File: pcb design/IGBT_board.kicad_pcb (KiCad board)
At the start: 4 copper layers, 150 x 100 mm, 238 parts, among them J1 4-794627-0, J2 DESAT, J3 DESAT, Q1 IGBT, Q10 IGBT, Q11 IGBT, Q12 IGBT, Q13 NPN, Q14 PNP, Q15 CSD19533Q5A, Q16 CSD19533Q5A, Q17 NPN, Q18 PNP, Q19 PNP, Q2 IGBT, Q20 PNP, Q3 IGBT, Q4 IGBT, Q5 IGBT, Q6 IGBT, Q7 IGBT, Q8 IGBT, Q9 IGBT, T1 TRANS-3-1CT, U1 ISO5852S, U11 TLP2745, U12 OPA2172, U2 LM5030, U3 ISO5852S, U4 NAND, U5 APE8865U5-33-HF-3, U6 NAND, U7 NAND, U8 TLP2745, U9 OPA2172

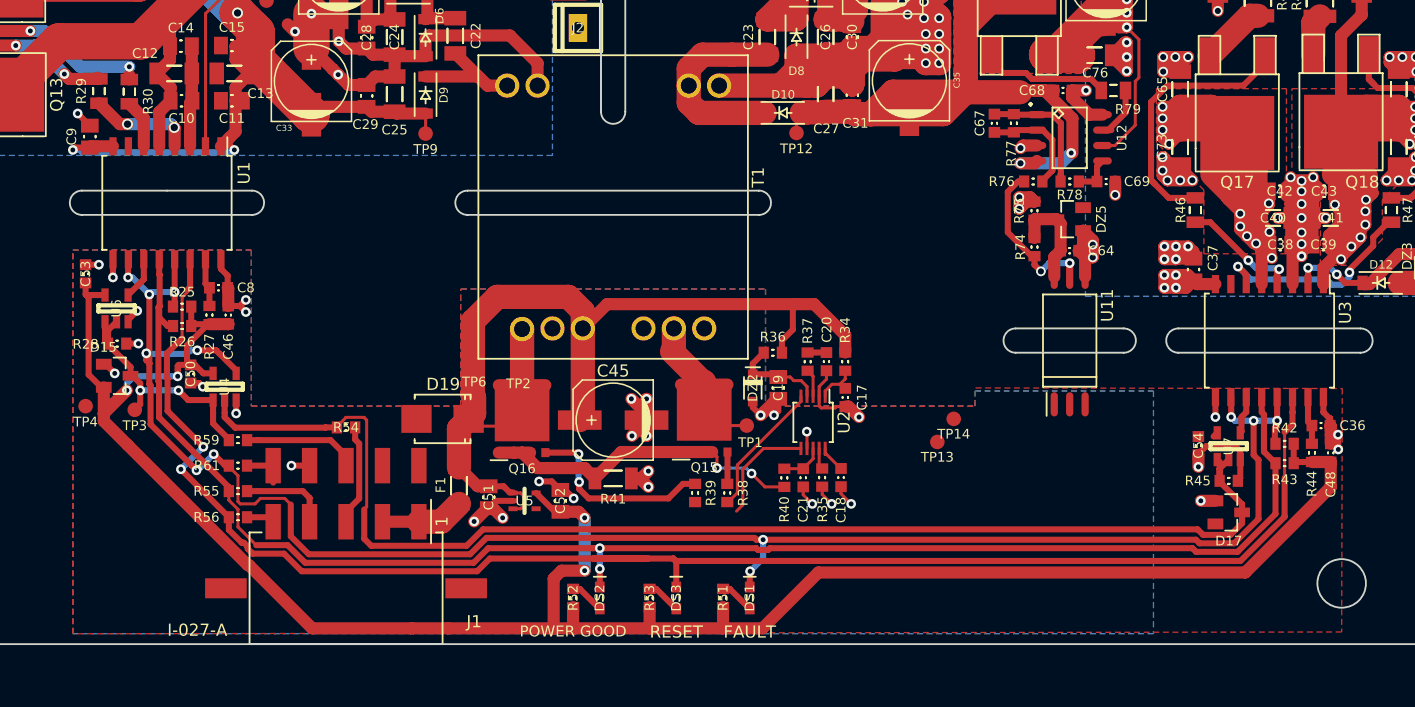
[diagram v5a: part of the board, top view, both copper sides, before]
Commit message: Phase voltage sensing laid out
Signed-off-by: Marcos Chaparro <mchaparro@paltatech.com>
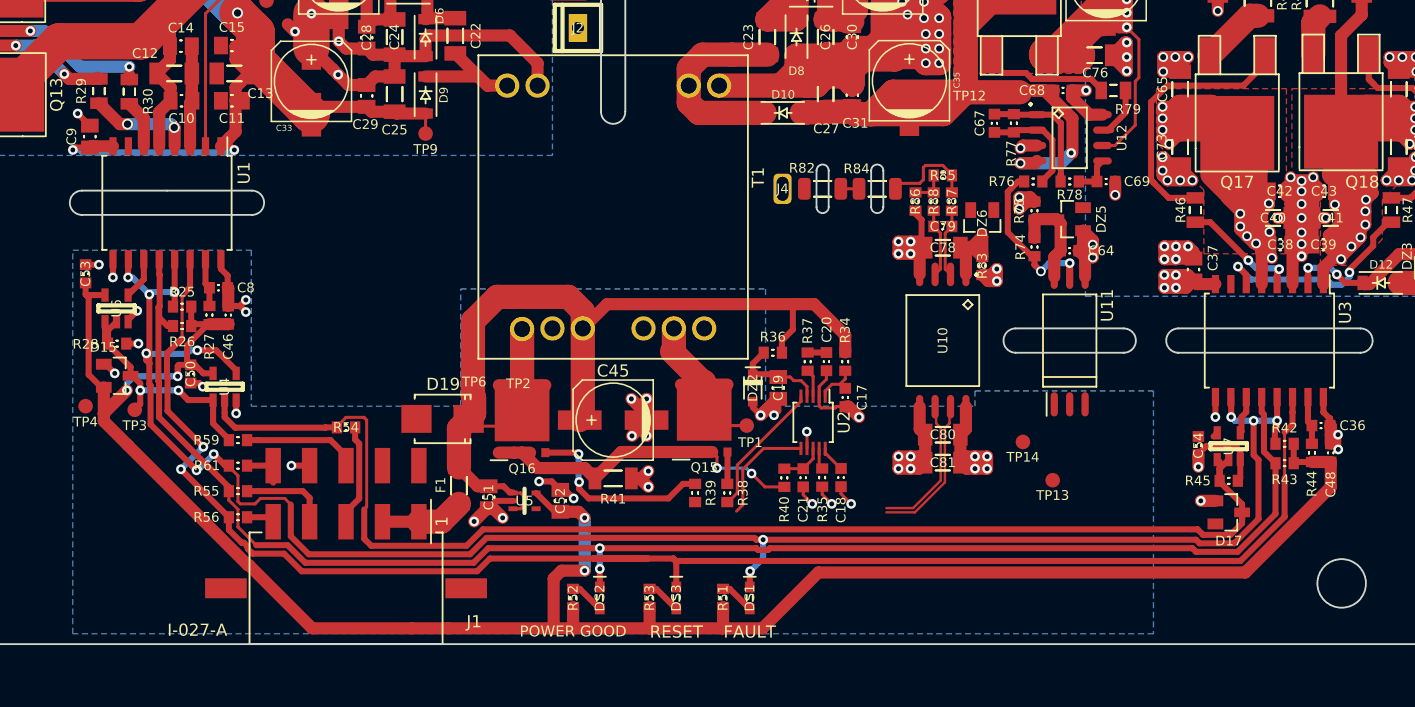
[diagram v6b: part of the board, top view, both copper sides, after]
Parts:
- added C78: 100nF, IPC7351-Nominal:CAPC3216X70, F.Cu at (27.1, 17.4)
- added C79: 330pF, IPC7351-Nominal:CAPC1608X55, F.Cu at (27.1, 15.6)
- added C80: 100nF, IPC7351-Nominal:CAPC3216X70, F.Cu at (27.1, 32.8)
- added C81: 1uF, IPC7351-Nominal:CAPC3216X70, F.Cu at (27.1, 35.0)
- added DZ6: 5v, smd-semi:SOT-23, F.Cu at (30.4, 15.3)
- added J4: PHASE, conn-100mil:CONN-100MIL-F-1x1, F.Cu at (13.9, 12.5)
- added R82: 1M, IPC7351-Nominal:RESC3216X60, F.Cu at (17.2, 12.5)
- added R83: 12R, IPC7351-Nominal:RESC1608X50, F.Cu at (30.4, 18.9)
- added R84: 1M, IPC7351-Nominal:RESC3216X60, F.Cu at (21.8, 12.5)
- added R85: 1k, IPC7351-Nominal:RESC1608X50, F.Cu at (27.1, 11.4)
- added R86: 10k, IPC7351-Nominal:RESC1608X50, F.Cu at (24.9, 13.6)
- added R87: 12R, IPC7351-Nominal:RESC1608X50, F.Cu at (27.9, 13.6)
- added R88: 12R, IPC7351-Nominal:RESC1608X50, F.Cu at (26.4, 13.6)
- added U10: AMC1200, IPC7351-Nominal:SOIC127P1032X265-8, F.Cu at (27.1, 25.0)
- moved TP12 14.9 mm to (29.4, 3.55)
- moved TP13 10.0 mm to (36.2, 36.5)
- moved TP14 6.01 mm to (33.8, 33.4)
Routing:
- net /phase voltage/Vout+: track 0.00 -> 12.3 mm
- net /phase voltage/Vout-: track 0.00 -> 11.7 mm
- net VBUS-: track 667.0 -> 678.6 mm, vias 71 -> 75
- net 3.3v: track 177.9 -> 188.5 mm, vias 4 -> 8
- net GND: track 72.1 -> 82.7 mm, vias 32 -> 36
- net Net-(C78-Pad2): track 0.00 -> 8.32 mm
- net Net-(R84-Pad1): track 0.00 -> 7.82 mm
- net /phase voltage/VIN-: track 0.00 -> 5.81 mm
- net /phase voltage/VIN+: track 0.00 -> 5.66 mm
- net /IGBT_driver_BOT/+15V: track 107.8 -> 111.7 mm, vias 22 -> 24
- net Net-(R85-Pad2): track 0.00 -> 2.90 mm
- net /IGBT_driver_BOT/-8V: track 68.0 -> 66.4 mm
- net Net-(R82-Pad1): track 0.00 -> 1.50 mm
- removed copper zone on F.Cu, net GND
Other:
- outline, holes or cut-outs redrawn

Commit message: Added mounting points, trying 12 pos connector. Added 3d models
Signed-off-by: Marcos Chaparro <mchaparro@paltatech.com>
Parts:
- removed C55, C63: 1nF, IPC7351-Nominal:CAPC1608X55
- removed C56: 1uF, IPC7351-Nominal:CAPC1608X55
- removed C57, C58, C71, C72, C75: 10uF 50v, IPC7351-Nominal:CAPC3216X70
- removed C59, C61: 10nF, IPC7351-Nominal:CAPC1608X55
- removed C60: 100nF, IPC7351-Nominal:CAPC1608X55
- removed C62: 47uF 50v, w_smd_cap:c_elec_6.3x7.7
- removed DS4: CAPS_CHARGED, smd-semi:LED-0603
- removed DZ4: 10v, smd-semi:SOT-23
- removed the G*** at (136.8, -17.4)
- removed J1: 4-794627-0, paltatech:TE-4-794627-0
- removed Q19: PNP, SMD_Packages:DPAK-2
- removed R62, R63, R66: 50k 1W, IPC7351-Nominal:RESC6432X70
- removed R68: 380R, IPC7351-Nominal:RESC1608X50
- removed R69: 470R, IPC7351-Nominal:RESC1608X50
- removed R70, R71, R72: 10k, IPC7351-Nominal:RESC1608X50
- removed R73: 100R, IPC7351-Nominal:RESC2012X50
- removed U8: TLP2745, paltatech:SDIP6
- removed U9: OPA2172, IPC7351-Nominal:SOIC127P600X175-8
- added HOLE102: MOUNTING_HOLE, paltatech:SMD_STANDOFF_M3, F.Cu at (-33.0, 45.0)
- added HOLE102: MOUNTING_HOLE, paltatech:SMD_STANDOFF_M3, F.Cu at (-58.0, 45.0)
- added REF**: inverter_support2, inverter_support2, F.Cu at (0.00, 50.0)
- added REF**: MountingHole_6mm, Mounting_Holes:MountingHole_4mm, F.Cu at (76.5, -32.0)
- added REF**: MountingHole_6mm, Mounting_Holes:MountingHole_4mm, F.Cu at (-76.5, -32.0)
- added REF**: Pin_Header_Straight_2x06, Pin_Headers:Pin_Header_Straight_2x06, F.Cu at (-51.9, 46.1)
- MP1: footprint paltatech:heatsink-watercooled-20x210mm -> heatsink-watercooled-20x210mm
- moved R60 20.1 mm to (-72.0, -17.9), turned to 0 degrees
- moved C47 15.5 mm to (-72.0, -20.4), turned to 180 degrees
- moved DZ2 7.73 mm to (13.6, 36.4)
- moved C21 3.90 mm to (15.6, 40.2)
- moved R40 3.90 mm to (14.1, 40.2)
- moved C20 3.90 mm to (17.5, 30.6)
- moved R34 3.90 mm to (19.1, 30.6)
- moved R37 3.90 mm to (16.0, 30.6)
- moved U2 3.90 mm to (16.4, 35.6)
- moved C17 3.90 mm to (19.1, 33.6)
- moved C18 3.90 mm to (18.7, 40.2)
- moved C19 3.90 mm to (13.6, 32.8)
- moved R35 3.90 mm to (17.2, 40.2)
- moved R36 3.90 mm to (13.1, 29.9)
- moved TP1 3.90 mm to (10.9, 35.9)
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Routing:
- net 24v: track 72.2 -> 42.8 mm
- net Net-(R48-Pad1): track 1.70 -> 13.9 mm
- net PHASE: track 300.0 -> 288.6 mm, vias 9 -> 7
- net Net-(R49-Pad1): track 1.70 -> 11.0 mm
- net VBUS-: track 678.6 -> 687.3 mm, vias 75 -> 76
- net Net-(R38-Pad2): track 11.3 -> 3.86 mm
- net /IGBT_driver_BOT/-VEE: track 110.9 -> 116.3 mm
- net (no net): track 0.00 -> 4.28 mm, vias 0 -> 4
- net GND: track 82.7 -> 78.6 mm, vias 36 -> 32
- net Net-(R39-Pad1): track 9.16 -> 8.44 mm
- net Net-(C19-Pad1): track 7.83 -> 8.33 mm, vias 0 -> 1
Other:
- board size 150 x 100 mm -> 162 x 100 mm

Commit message: Added comments before I forget things, changed X5R to X7R. Updated PCB
Signed-off-by: Marcos Chaparro <mchaparro@paltatech.com>
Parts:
- added C55: 1nF, IPC7351-Nominal:CAPC1608X55, F.Cu at (181.2, 24.1)
- added C56: 1uF, IPC7351-Nominal:CAPC1608X55, F.Cu at (165.7, 41.0)
- added C57: 10uF 50v, IPC7351-Nominal:CAPC3216X70, F.Cu at (151.2, 40.3)
- added C58: 10uF 50v, IPC7351-Nominal:CAPC3216X70, F.Cu at (158.9, 33.7)
- added C59: 10nF, IPC7351-Nominal:CAPC1608X55, F.Cu at (172.4, 3.87)
- added C60: 100nF, IPC7351-Nominal:CAPC1608X55, F.Cu at (178.9, -1.13)
- added C61: 10nF, IPC7351-Nominal:CAPC1608X55, F.Cu at (170.8, 10.5)
- added C62: 47uF 50v, w_smd_cap:c_elec_6.3x7.7, F.Cu at (163.4, 2.45)
- added C63: 1nF, IPC7351-Nominal:CAPC1608X55, F.Cu at (134.1, 38.9)
- added C71: 10uF 50v, IPC7351-Nominal:CAPC3216X70, F.Cu at (166.7, 24.5)
- added C72: 10uF 50v, IPC7351-Nominal:CAPC3216X70, F.Cu at (166.7, 29.8)
- added C75: 10uF 50v, IPC7351-Nominal:CAPC3216X70, F.Cu at (151.2, 15.2)
- added C77: 100pF, IPC7351-Nominal:CAPC1608X55, F.Cu at (131.1, 30.9)
- added C82: 100pF, IPC7351-Nominal:CAPC1608X55, F.Cu at (137.0, 30.9)
- added C83: 100nF, IPC7351-Nominal:CAPC1608X55, F.Cu at (173.5, 30.3)
- added C84: 100nF, IPC7351-Nominal:CAPC1608X55, F.Cu at (134.1, 43.4)
- added DS4: CAPS_CHARGED, smd-semi:LED-0603, F.Cu at (122.0, 31.0)
- added Q19: PNP, SMD_Packages:DPAK-2, F.Cu at (152.4, 9.29)
- added R62: 50k 1W, IPC7351-Nominal:RESC6432X70, F.Cu at (133.0, 7.05)
- added R63: 50k 1W, IPC7351-Nominal:RESC6432X70, F.Cu at (133.0, 14.0)
- added R66: 50k 1W, IPC7351-Nominal:RESC6432X70, F.Cu at (133.0, 0.10)
- added R68: 380R, IPC7351-Nominal:RESC1608X50, F.Cu at (173.4, 34.8)
- added R69: NI, IPC7351-Nominal:RESC3216X60, F.Cu at (166.6, 35.6)
- added R70: 10k, IPC7351-Nominal:RESC1608X50, F.Cu at (176.8, 8.40)
- added R71: 10k, IPC7351-Nominal:RESC1608X50, F.Cu at (178.9, 3.40)
- added R72: 10k, IPC7351-Nominal:RESC1608X50, F.Cu at (170.8, 15.0)
- added R73: 100R, IPC7351-Nominal:RESC2012X50, F.Cu at (172.7, -0.88)
- added R80: NI, IPC7351-Nominal:RESC3216X60, F.Cu at (174.4, 24.9)
- added R81: NI, IPC7351-Nominal:RESC3216X60, F.Cu at (158.9, 39.5)
- added R89: NI, IPC7351-Nominal:RESC3216X60, F.Cu at (52.2, -3.25)
- added R90: NI, IPC7351-Nominal:RESC3216X60, F.Cu at (59.1, -3.25)
- added R91: NI, IPC7351-Nominal:RESC3216X60, F.Cu at (52.2, -7.85)
- added R92: NI, IPC7351-Nominal:RESC3216X60, F.Cu at (59.1, -7.85)
- added U13: LM3480, smd-semi:SOT-23, F.Cu at (151.2, 34.3)
- added U8: TLP2745, paltatech:SDIP6, F.Cu at (155.1, 25.6)
- added U9: OPA2172, IPC7351-Nominal:SOIC127P600X175-8, F.Cu at (162.6, 12.9)
- C16, C44: value 100pF -> 100pF COG
- D13, D14, D3, D4: value GL41Y-E3/96 -> MURS160-13-F; footprint paltatech:melf-DO-213AB -> Diodes_SMD:Diode-SMB_Standard
- MP1: footprint heatsink-watercooled-20x210mm -> paltatech:heatsink-watercooled-20x210mm
- R28, R45: value 10k -> 4.7k
- R29, R30, R46, R47: value 10R -> 0R5
- R31, R32, R48, R49, R57, R58, R64, R65: footprint IPC7351-Nominal:RESC3225X60 -> IPC7351-Nominal:RESC3216X60
- R75: value 470R -> NI; footprint IPC7351-Nominal:RESC1608X50 -> IPC7351-Nominal:RESC3216X60
- U14: renamed from DZ5; value 10v -> LM3480
- moved R65 1.41 mm to (56.8, -7.85)
- moved R49 1.41 mm to (56.8, -3.25)
- moved R64 1.40 mm to (54.5, -7.85)
- moved R48 1.40 mm to (54.5, -3.25)
- moved D14 0.60 mm to (71.8, 4.50)
- moved D18 0.45 mm to (49.4, -5.55)
- moved D11 0.30 mm to (62.0, -5.55)
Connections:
- C64 pad 1: Net-(C64-Pad1) -> /IGBT_driver_BOT/12.0V
- R74 pad 2: Net-(C64-Pad1) -> /IGBT_driver_BOT/12.0V
- R75 pad 1: /IGBT_driver_BOT/+15V -> Net-(R32-Pad1)
- R75 pad 2: Net-(C64-Pad1) -> Net-(Q14-Pad3)
- U11 pad 6: Net-(C64-Pad1) -> /IGBT_driver_BOT/12.0V
- U14 pad 1: VBUS- -> /IGBT_driver_BOT/12.0V
- U14 pad 2: (no net) -> /IGBT_driver_BOT/+15V
- U14 pad 3: Net-(C64-Pad1) -> VBUS-
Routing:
- net 3.3v: track 188.5 -> 158.7 mm
- net GND: track 78.6 -> 108.5 mm
- net Net-(C64-Pad1): track 8.43 -> 0.00 mm
- net /IGBT_driver_BOT/+15V: track 111.7 -> 104.8 mm, vias 24 -> 20
- net GATE_LOW: track 533.4 -> 539.8 mm
- net VBUS-: track 687.3 -> 693.6 mm
- net /IGBT_driver_BOT/12.0V: track 0.00 -> 5.00 mm
- net Net-(R32-Pad1): track 1.70 -> 5.54 mm, vias 0 -> 2
